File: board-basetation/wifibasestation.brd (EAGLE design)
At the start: 49.8 x 22 mm, 33 parts, among them IC1 1117EMP, IC2 STM32F072, IC3 HTU21D, J1 SWD_SHROUD_SMD, X1 ESP-03, X2 SMA-142-0711-821/826

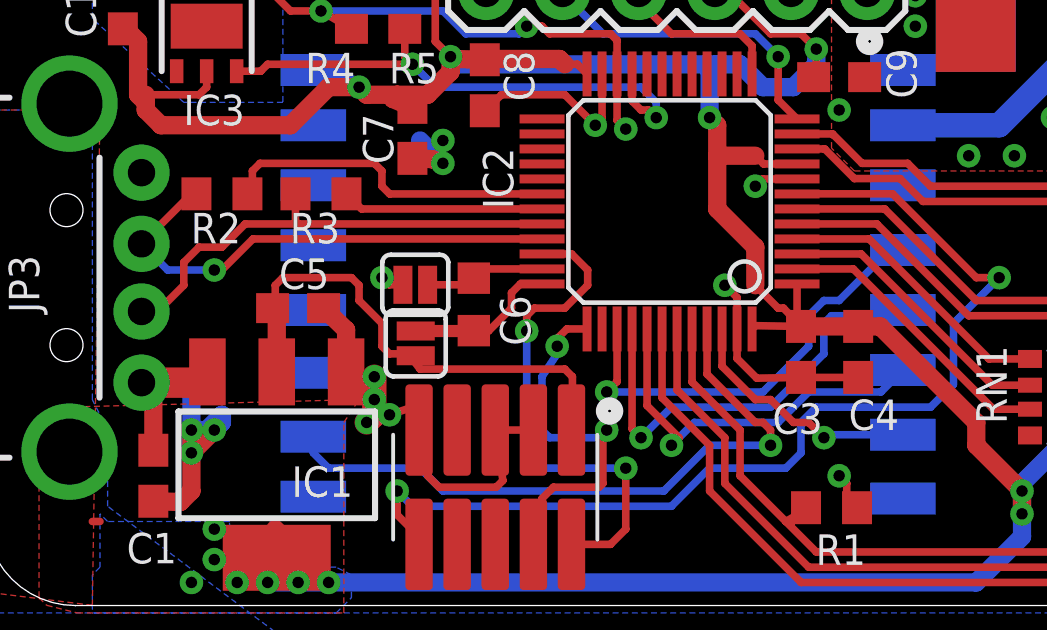
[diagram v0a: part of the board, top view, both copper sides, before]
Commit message: increasing cap package size
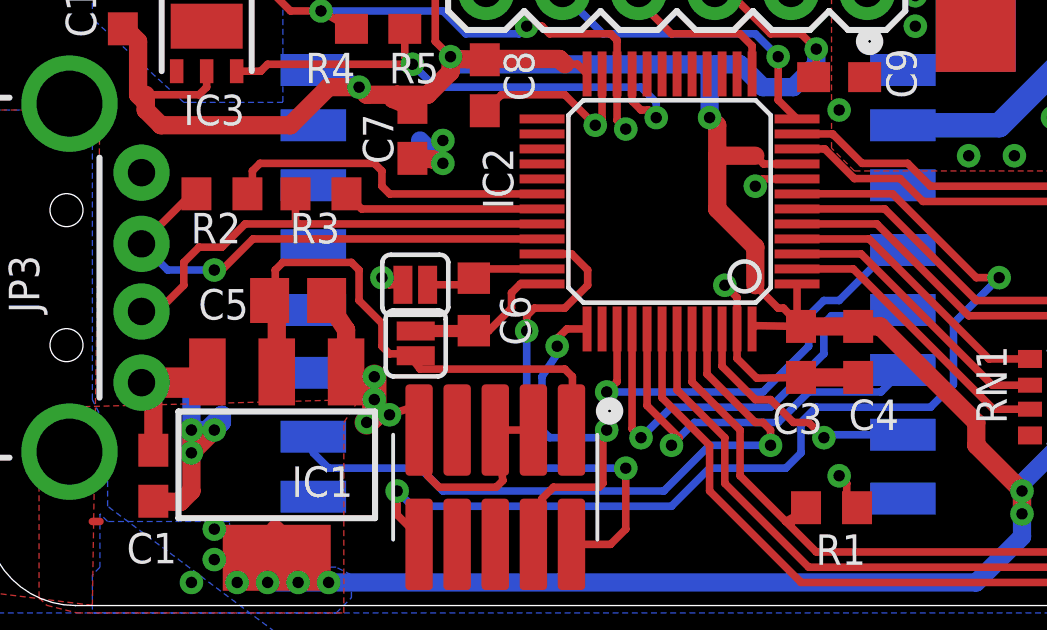
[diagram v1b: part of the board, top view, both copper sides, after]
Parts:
- C5: device rcl:C0603 -> rcl:C0805
- moved C5 0.25 mm to (10.7, 10.7)
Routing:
- net +3V3: track 146.9 -> 148.3 mm
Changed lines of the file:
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@@
 <layer number="27" name="tValues" color="7" fill="1" visible="yes" active="yes"/>
 <layer number="28" name="bValues" color="7" fill="1" visible="yes" active="yes"/>
-<layer number="29" name="tStop" color="7" fill="3" visible="yes" active="yes"/>
-<layer number="30" name="bStop" color="7" fill="6" visible="yes" active="yes"/>
-<layer number="31" name="tCream" color="7" fill="4" visible="yes" active="yes"/>
-<layer number="32" name="bCream" color="7" fill="5" visible="yes" active="yes"/>
+<layer number="29" name="tStop" color="7" fill="3" visible="no" active="yes"/>
+<layer number="30" name="bStop" color="7" fill="6" visible="no" active="yes"/>
+<layer number="31" name="tCream" color="7" fill="4" visible="no" active="yes"/>
+<layer number="32" name="bCream" color="7" fill="5" visible="no" active="yes"/>
 <layer number="33" name="tFinish" color="6" fill="3" visible="no" active="yes"/>
 <layer number="34" name="bFinish" color="6" fill="6" visible="no" active="yes"/>
@@
 <attribute name="NAME" x="4.953" y="1.905" size="1.016" layer="25" font="vector" ratio="14"/>
 </element>
-<element name="C5" library="rcl" package="C0603" value="4u7" x="10.668" y="10.414" smashed="yes">
-<attribute name="NAME" x="10.033" y="11.049" size="1.016" layer="25" font="vector" ratio="14"/>
+<element name="C5" library="rcl" package="C0805" value="4u7" x="10.668" y="10.668" smashed="yes">
+<attribute name="NAME" x="9.017" y="11.049" size="1.016" layer="25" font="vector" ratio="14" rot="R180"/>
 </element>
 <element name="C2" library="rcl" package="C0603" value="1u" x="48.114" y="6.267" smashed="yes" rot="R90">
@@
 <contactref element="LED2" pad="C"/>
 <contactref element="LED3" pad="C"/>
-<wire x1="29.337" y1="8.104" x2="27.432" y2="8.104" width="0.254" layer="1"/>
 <wire x1="27.432" y1="8.104" x2="25.957" y2="8.079" width="0.254" layer="1"/>
 <wire x1="25.3" y1="9.72" x2="25.3" y2="8.736" width="0.254" layer="1"/>
@@
 <wire x1="12.2674" y1="8.2888" x2="12.2674" y2="9.6896" width="0.6096" layer="1"/>
 <via x="13.208" y="8.128" extent="1-16" drill="0.381" shape="octagon"/>
-<wire x1="12.2674" y1="9.6896" x2="11.518" y2="10.414" width="0.6096" layer="1"/>
+<wire x1="12.2674" y1="9.6896" x2="11.618" y2="10.668" width="0.6096" layer="1"/>
 <wire x1="5.842" y1="3.976" x2="6.745" y2="3.951" width="0.6096" layer="1"/>
 <wire x1="6.745" y1="3.951" x2="7.112" y2="4.318" width="0.6096" layer="1"/>
@@
 <via x="31.242" y="21.844" extent="1-16" drill="0.381" shape="octagon"/>
 <wire x1="48.756" y1="8.128" x2="55.88" y2="15.494" width="0" layer="19" extent="1-1"/>
+<wire x1="29.337" y1="8.104" x2="27.432" y2="8.104" width="0.6096" layer="1"/>
 </signal>
 <signal name="+3V3">
@@
 <wire x1="13.829" y1="17.385" x2="13.97" y2="17.526" width="0.6096" layer="1"/>
 <wire x1="9.956" y1="8.2888" x2="9.956" y2="10.251" width="0.6096" layer="1"/>
-<wire x1="9.956" y1="10.251" x2="9.818" y2="10.414" width="0.6096" layer="1"/>
-<wire x1="12.446" y1="11.43" x2="10.16" y2="11.43" width="0.254" layer="1"/>
-<wire x1="10.16" y1="11.43" x2="9.906" y2="11.176" width="0.254" layer="1"/>
-<wire x1="9.906" y1="11.176" x2="9.906" y2="10.527" width="0.254" layer="1"/>
-<wire x1="9.906" y1="10.527" x2="9.818" y2="10.414" width="0.254" layer="1"/>
+<wire x1="9.956" y1="10.251" x2="9.718" y2="10.668" width="0.6096" layer="1"/>
+<wire x1="12.446" y1="11.938" x2="10.16" y2="11.938" width="0.254" layer="1"/>
+<wire x1="10.16" y1="11.938" x2="9.906" y2="11.684" width="0.254" layer="1"/>
+<wire x1="9.906" y1="11.684" x2="9.906" y2="10.527" width="0.254" layer="1"/>
+<wire x1="9.906" y1="10.527" x2="9.718" y2="10.668" width="0.254" layer="1"/>
 <polygon width="0.254" layer="1" isolate="0.254" thermals="no">
 <vertex x="3.302" y="0.254"/>
@@
 <wire x1="14.732" y1="8.382" x2="19.558" y2="8.382" width="0.254" layer="1"/>
 <wire x1="19.558" y1="8.382" x2="19.812" y2="8.128" width="0.254" layer="1"/>
-<wire x1="12.446" y1="11.43" x2="12.7" y2="11.176" width="0.254" layer="1"/>
-<wire x1="12.7" y1="11.176" x2="12.7" y2="10.668" width="0.254" layer="1"/>
+<wire x1="12.446" y1="11.938" x2="12.7" y2="11.684" width="0.254" layer="1"/>
+<wire x1="12.7" y1="11.684" x2="12.7" y2="10.668" width="0.254" layer="1"/>
 <wire x1="12.7" y1="10.668" x2="13.462" y2="9.906" width="0.254" layer="1"/>
 <wire x1="13.462" y1="9.906" x2="13.462" y2="9.144" width="0.254" layer="1"/>

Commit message: almost done
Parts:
- added R6: 1k, passives-7351:R0603-N
- added U$3: ESP-07, Mine:ESP-07
- added X3: LTI-SASF54GT, con-coax:LTI-SASF54GT
- added X4: SMA-142-0711-821/826, con-coax:J502-ND-142-0711-821/826
- added X5: SMA-142-0711-871/876, con-coax:J502-ND-142-0711-871/876
- added X6: BU-SMA-V, con-coax:BU-SMA-V
- C1, C10, C2, C3, C4, C7, C8, C9: device rcl:C0603 -> passives-7351:C0603-N
- C5: device rcl:C0805 -> passives-7351:C0805-N
- C6: device rcl:C0603K -> passives-7351:C0603-N
- R1, R2, R3, R4, R5: device rcl:R0603 -> passives-7351:R0603-N
- moved C2 1.37 mm to (48.6, 5.00)
- moved X1 0.92 mm to (35.6, 2.03)
- moved X2 0.25 mm to (36.8, 22.8)
- moved J1 0.25 mm to (17.2, 4.19)
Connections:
- new net N$1: R6.2, U$3.6, X1.6
- new net N$3: U$3.2, X1.2
- new net N$4: U$3.4, X1.4
- new net N$7: U$3.3, X1.3
- net +3V3: now also R6.1, U$3.1
- net CH_PD: now also U$3.13
- net GND: now also U$3.8
- net GPIO0: now also U$3.7
- net GPIO15: now also U$3.5
- net USART1_RX: now also U$3.10
- net USART1_TX: now also U$3.11
- net W_RST: now also U$3.12
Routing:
- net N$1: track 0.00 -> 5.50 mm, vias 0 -> 1
- net W_RST: track 21.3 -> 24.9 mm
- net +3V3: track 148.3 -> 151.6 mm
- net CH_PD: track 23.2 -> 26.2 mm
- net USART1_RX: track 41.2 -> 44.2 mm
- net USART1_TX: track 41.5 -> 43.6 mm
- net GPIO0: track 38.2 -> 40.0 mm
- net N$7: track 0.00 -> 0.76 mm
- net N$4: track 0.00 -> 0.76 mm
- net N$3: track 0.00 -> 0.76 mm
- net GND: track 58.6 -> 58.4 mm, vias 33 -> 48
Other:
- board size 49.8 x 22 mm -> 49.8 x 22.5 mm
- board text added: "Add tape to insulate vias"
- board text added: "BOOT"
- board text added: "Jan 2015"
- board text added: "Matt Brejza"
- board text added: "©"

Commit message: routed RST
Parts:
- removed SV1: (no value), con-lstb:MA04-2
- removed U$1: LMT85, Mine:SC70-5L
- removed X3: LTI-SASF54GT, con-coax:LTI-SASF54GT
- removed X4: SMA-142-0711-821/826, con-coax:J502-ND-142-0711-821/826
- removed X5: SMA-142-0711-871/876, con-coax:J502-ND-142-0711-871/876
- removed X6: BU-SMA-V, con-coax:BU-SMA-V
- moved C6 0.51 mm to (17.0, 10.5)
- moved JP1 0.51 mm to (15.1, 9.24)
- moved JP2 0.51 mm to (15.1, 11.2)
- moved J1 0.25 mm to (17.2, 3.94)
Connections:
- removed net N$5: SV1.5
- net +3V3: no longer SV1.2
- net CH_PD: no longer SV1.6
- net GND: no longer SV1.7
- net GPIO0: no longer SV1.3
- net RST: now also IC2.38
- net USART1_RX: no longer SV1.8
- net USART1_TX: no longer SV1.1
- net W_RST: no longer SV1.4
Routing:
- net RST: track 0.00 -> 13.7 mm, vias 0 -> 1
- net MOSI: track 13.2 -> 14.4 mm
- net +3V3: track 151.6 -> 152.6 mm, vias 15 -> 16
- net MISO: track 14.7 -> 15.7 mm
- net GND: track 58.4 -> 59.3 mm, vias 48 -> 52
- net DIO0: track 21.5 -> 22.5 mm

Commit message: adding stencil and couple of values
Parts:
- R6: value 1k -> 4k7
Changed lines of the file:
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@@
 <attribute name="NAME" x="37.338" y="1.016" size="1.016" layer="25" font="vector" ratio="14"/>
 </element>
-<element name="R6" library="passives-7351" package="R0603-N" value="1k" x="35.814" y="4.572" smashed="yes">
+<element name="R6" library="passives-7351" package="R0603-N" value="4k7" x="35.814" y="4.572" smashed="yes">
 <attribute name="NAME" x="35.179" y="2.794" size="1.016" layer="25" font="vector" ratio="14"/>
 </element>

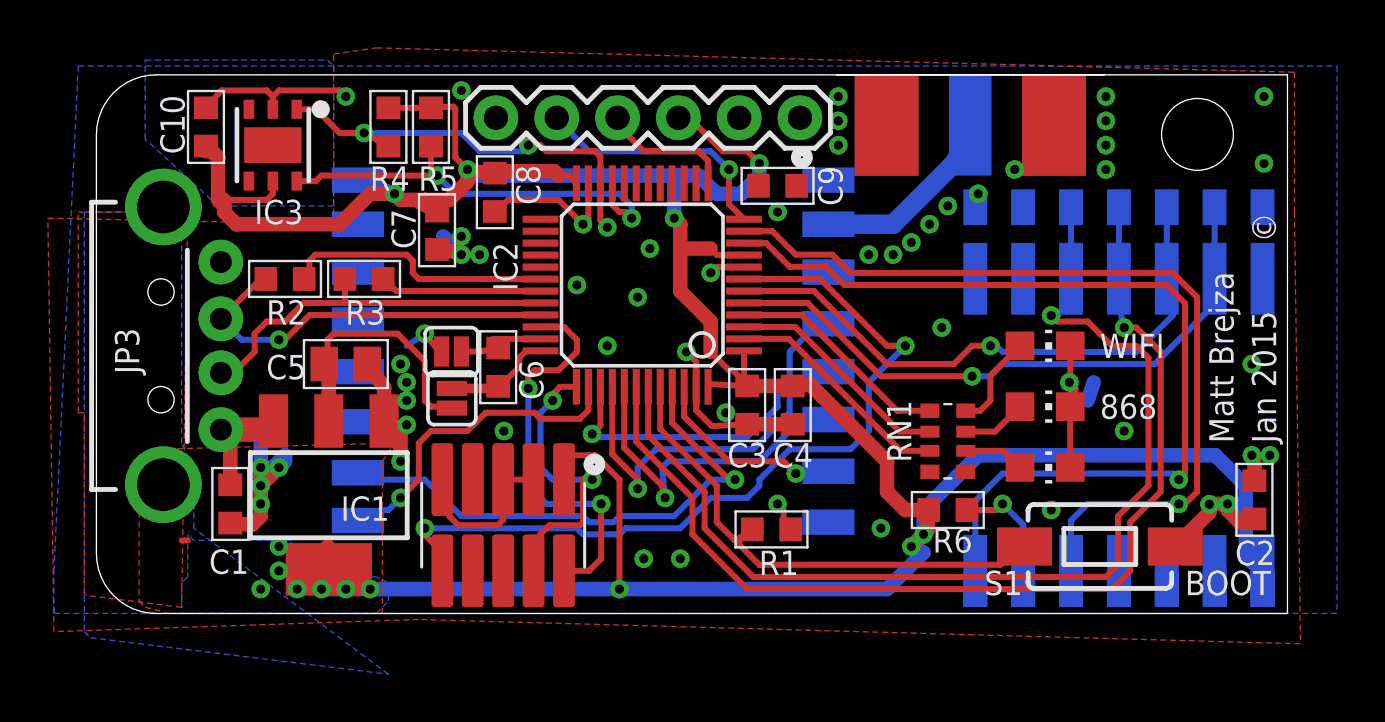
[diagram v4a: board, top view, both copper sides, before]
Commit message: HARDWARE: removes FTDI, HTU21
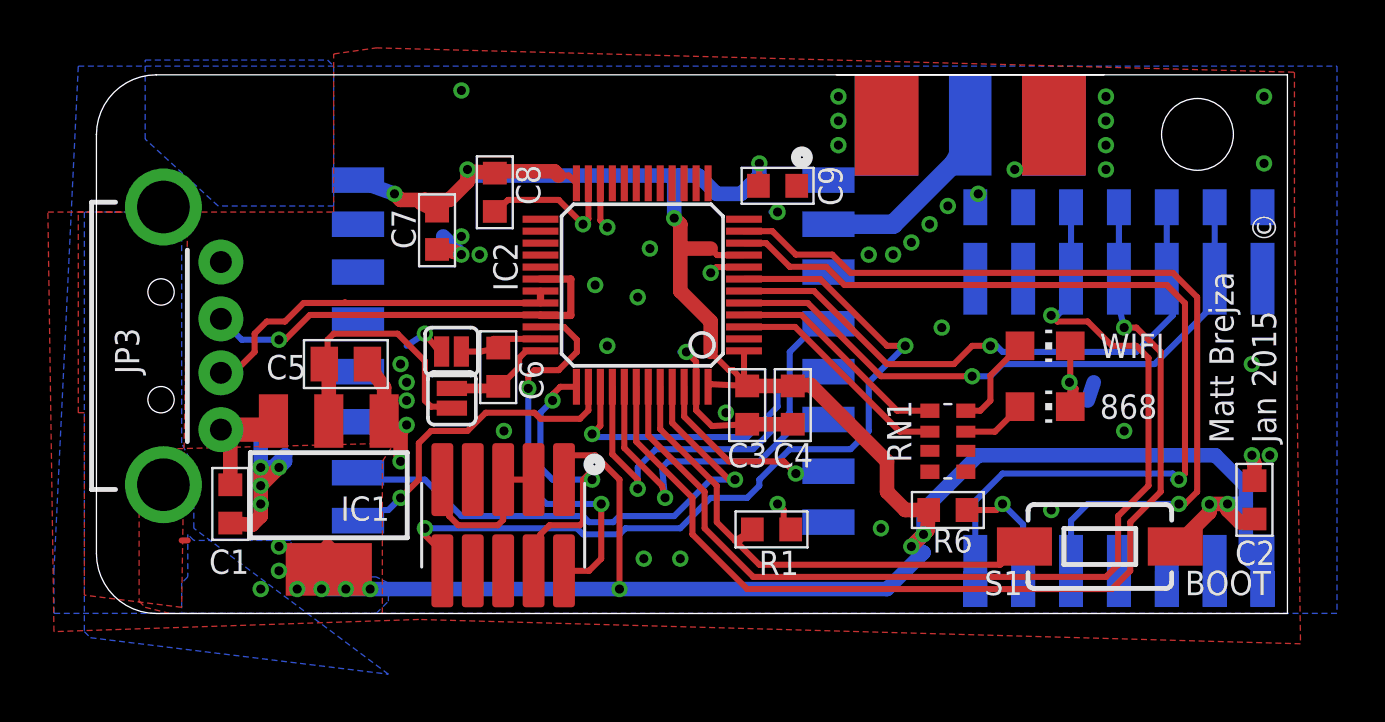
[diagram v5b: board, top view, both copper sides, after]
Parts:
- removed C10: 1u, passives-7351:C0603-N
- removed IC3: HTU21D, Mine:DFN6-L
- removed JP4: FTDI_BASICPTH, SparkFun-Connectors:FTDI_BASIC
- removed LED1: (no value), led:CHIP-LED0805
- removed R2: 10k, passives-7351:R0603-N
- removed R3: 100k, passives-7351:R0603-N
- removed R4, R5: 4k7, passives-7351:R0603-N
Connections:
- removed net N$17: IC2.31, R3.1
- removed net N$18: IC2.30, R2.1
- removed net N$2: IC2.2, RN1.3
- removed net N$20: LED1.A, RN1.6
- removed net USART2_RX: IC2.13, JP4.TXO
- removed net USART2_TX: IC2.12, JP4.RXI
- net +3V3: no longer C10.1, IC3.5, JP4.VCC, R4.2, R5.2
- net DM: now also IC2.31; no longer R3.2
- net DP: now also IC2.30; no longer R2.2
- net GND: no longer C10.2, IC3.2, JP4.GND, LED1.C
- net I2C2_SCL: no longer IC3.6, R5.1
- net I2C2_SDA: no longer IC3.1, R4.1
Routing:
- net +3V3: track 152.6 -> 128.9 mm
- net I2C2_SCL: track 18.4 -> 0.00 mm, vias 2 -> 0
- net I2C2_SDA: track 18.1 -> 2.08 mm, vias 3 -> 1
- net N$18: track 11.3 -> 0.00 mm
- net USART2_TX: track 10.5 -> 0.00 mm, vias 1 -> 0
- net N$2: track 9.70 -> 0.00 mm
- net GND: track 59.3 -> 49.8 mm, vias 52 -> 51
- net N$17: track 6.76 -> 0.00 mm
- net USART2_RX: track 5.64 -> 0.00 mm
- net N$20: track 2.55 -> 0.00 mm
- net DP: track 16.7 -> 18.2 mm
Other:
- board text removed: "G"
- board text removed: "IC3"
- board text removed: "R"
- board text removed: "T"
- board text removed: "V"

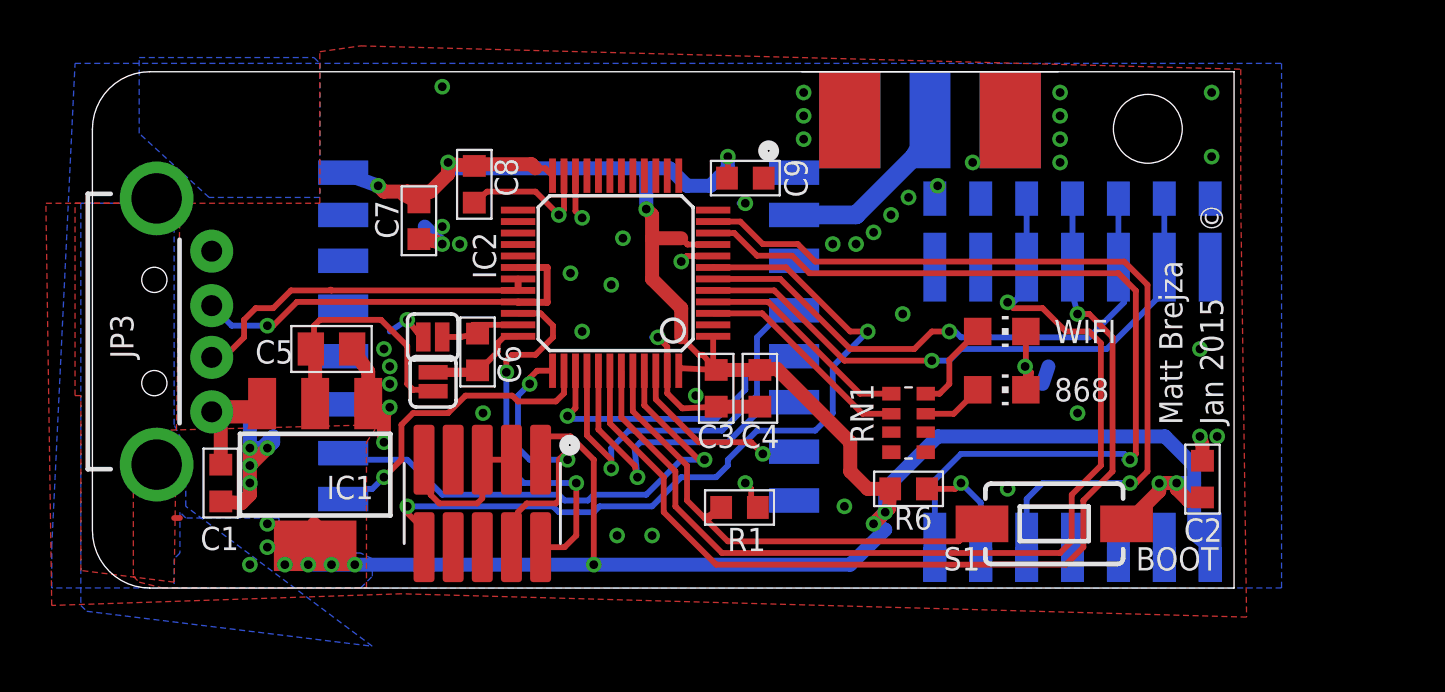
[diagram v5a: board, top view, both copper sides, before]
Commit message: HARDWARE: switch to ESP12
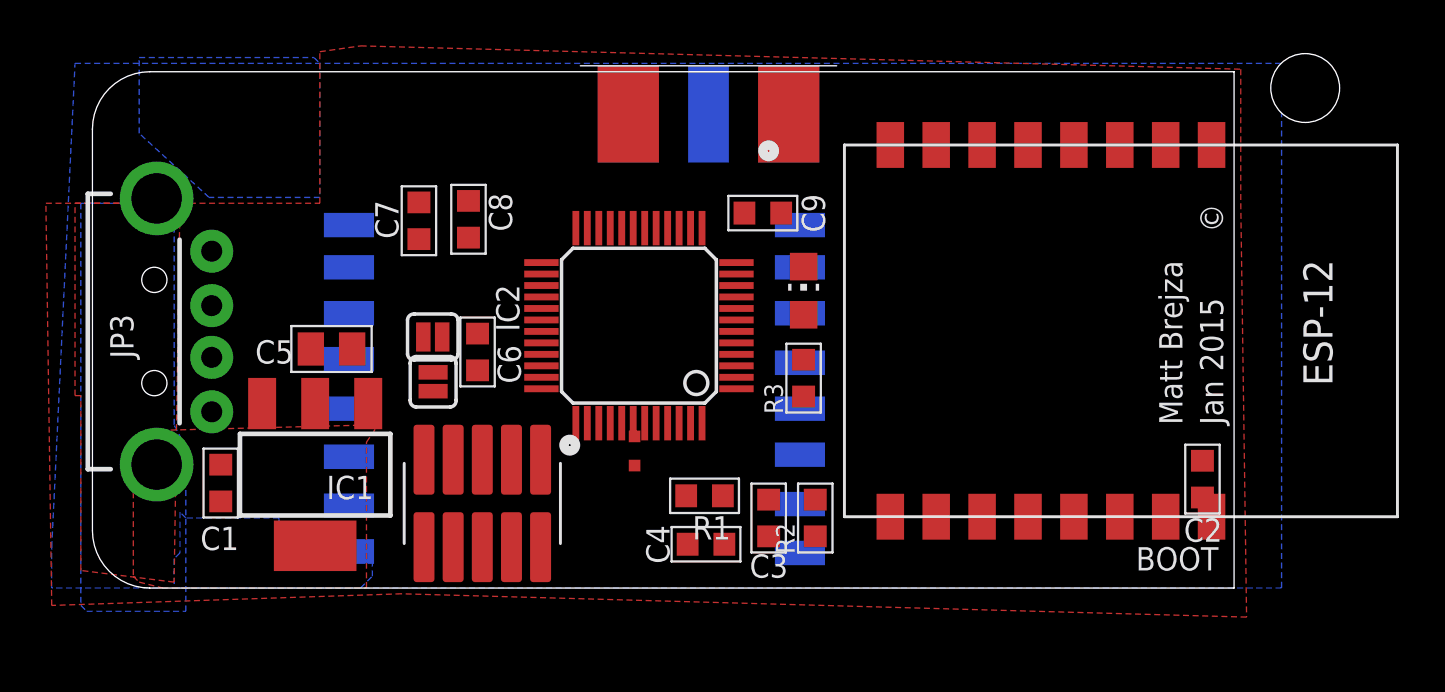
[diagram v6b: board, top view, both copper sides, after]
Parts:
- removed LED2: (no value), led:CHIP-LED0805
- removed R6: 4k7, passives-7351:R0603-N
- removed RN1: 330, resistor-dil:EXB38V
- removed S1: SWITCH-MOMENTARY-2SMD-1101NE, SparkFun-Electromechanical:TACTILE-SWITCH-1101NE
- removed U$3: ESP-07, Mine:ESP-07
- removed X1: ESP-03, Mine:ESP-03
- added R2, R3: (no value), passives-7351:R0603-N
- added TP1, TP2: TEST-POINT2, SparkFun-Connectors:PAD.02X.02
- added U$1: ESP8266_ESP-12, ESP8266-ESP12:ESP8266-ESP12
- moved X2 9.66 mm to (27.1, 23.0)
- moved LED3 8.82 mm to (31.2, 13.2), turned to 0 degrees
- moved C4 7.19 mm to (27.0, 2.16), turned to 180 degrees
- moved C3 6.10 mm to (29.7, 3.30)
- moved IC2 2.50 mm to (24.1, 11.7)
- moved U$2 2.30 mm to (11.4, 17.1)
- moved C9 1.70 mm to (29.5, 16.6)
- moved R1 1.61 mm to (26.9, 4.27)
- moved C8 1.55 mm to (16.6, 16.3)
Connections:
- removed net N$10: LED2.A, RN1.7
- removed net N$21: IC2.3, RN1.2
- removed net N$3: U$3.2, X1.2
- removed net N$4: U$3.4, X1.4
- removed net N$7: U$3.3, X1.3
- new net N$20: U$1.9
- net +3V3: now also R2.2, TP1.P$1, U$1.16; no longer R6.1, S1.2, U$3.1, X1.1
- net CH_PD: now also U$1.11; no longer U$3.13, X1.13
- net GND: now also U$1.1; no longer LED2.C, U$3.8, X1.8
- net GPIO0: no longer U$3.7, X1.7
- net GPIO15: now also U$1.2; no longer U$3.5, X1.5
- net N$1: now also R2.1, U$1.3; no longer R6.2, U$3.6, X1.6
- net N$15: now also TP2.P$1; no longer S1.1
- net N$22: now also R3.1; no longer RN1.1
- net N$9: now also R3.2; no longer RN1.8
- net USART1_RX: now also U$1.8; no longer U$3.10, X1.10
- net USART1_TX: now also U$1.7; no longer U$3.11, X1.11
- net W_RST: no longer U$3.12, X1.12
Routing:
- net +3V3: track 128.9 -> 0.00 mm, vias 16 -> 0
- net GND: track 49.8 -> 0.00 mm, vias 51 -> 0
- net USART1_RX: track 44.2 -> 0.00 mm, vias 1 -> 0
- net USART1_TX: track 43.6 -> 0.00 mm, vias 1 -> 0
- net GPIO0: track 40.0 -> 0.00 mm, vias 1 -> 0
- net GPIO15: track 36.8 -> 0.00 mm, vias 1 -> 0
- net NRST: track 34.7 -> 0.00 mm, vias 2 -> 0
- net CH_PD: track 26.2 -> 0.00 mm, vias 1 -> 0
- net W_RST: track 24.9 -> 0.00 mm, vias 1 -> 0
- net DIO0: track 22.5 -> 0.00 mm, vias 1 -> 0
- net N$15: track 22.0 -> 0.00 mm
- net DP: track 18.2 -> 0.00 mm, vias 1 -> 0
- net SWDAT: track 16.7 -> 0.00 mm, vias 2 -> 0
- net MISO: track 15.7 -> 0.00 mm, vias 1 -> 0
- net DM: track 15.6 -> 0.00 mm
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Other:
- board text removed: "868"
- board text removed: "WIFI"
